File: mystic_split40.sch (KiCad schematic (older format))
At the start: 4 parts

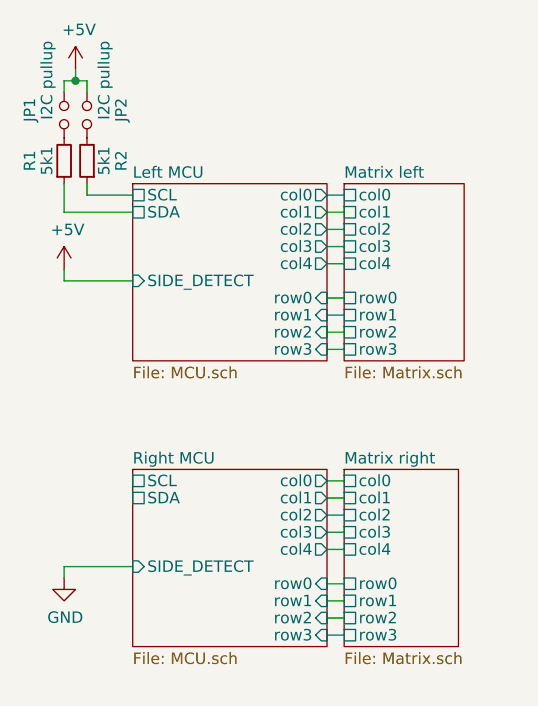
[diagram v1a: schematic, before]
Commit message: Copied left half layout to right components
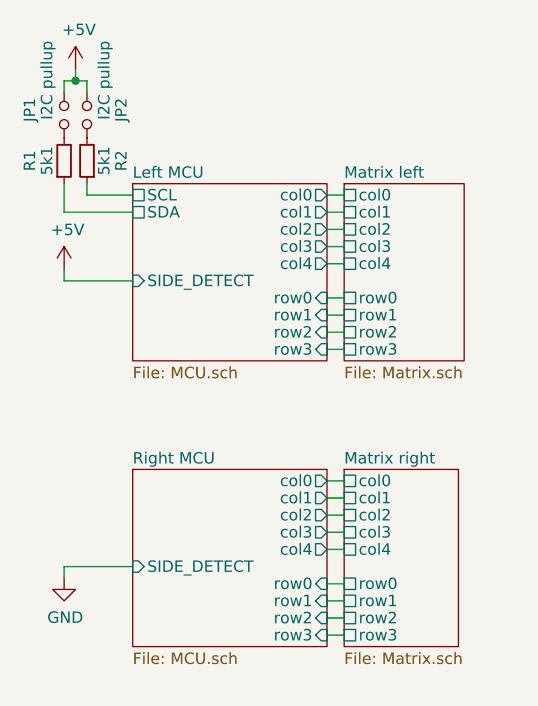
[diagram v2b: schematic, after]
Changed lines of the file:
@@
 F10 "row3" I R 5375 4775 50
 F11 "SIDE_DETECT" I L 4525 4475 50
-F12 "SCL" U L 4525 4100 50
-F13 "SDA" U L 4525 4175 50
 $EndSheet
 $Sheet

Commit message: Started work on adding extra col
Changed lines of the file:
@@
 $EndDescr
-Wire Wire Line
-	5375 3300 5450 3300
 Wire Wire Line
 	5375 3375 5450 3375
@@
 	0    1    1    0
 $EndComp
-$Sheet
-S 4525 2800 850  775
+Wire Wire Line
+	4325 2800 4325 2850
+Wire Wire Line
+	4325 2850 4525 2850
+Wire Wire Line
+	4525 2925 4225 2925
+Wire Wire Line
+	4225 2925 4225 2800
+Wire Wire Line
+	4225 3175 4225 3225
+$Sheet
+S 4525 4050 850  850
+U 5E0F7128
+F0 "Right MCU" 50
+F1 "MCU.sch" 50
+F2 "col0" O R 5375 4100 50
+F3 "col1" O R 5375 4175 50
+F4 "col2" O R 5375 4250 50
+F5 "col3" O R 5375 4325 50
+F6 "col4" O R 5375 4400 50
+F7 "row0" I R 5375 4625 50
+F8 "row1" I R 5375 4700 50
+F9 "row2" I R 5375 4775 50
+F10 "row3" I R 5375 4850 50
+F11 "SIDE_DETECT" I L 4525 4475 50
+F12 "col5" O R 5375 4475 50
+$EndSheet
+$Sheet
+S 5450 2800 525  850
+U 5DBF64D6
+F0 "Matrix left" 50
+F1 "Matrix.sch" 50
+F2 "col0" U L 5450 2850 50
+F3 "col1" U L 5450 2925 50
+F4 "col2" U L 5450 3000 50
+F5 "col3" U L 5450 3075 50
+F6 "col4" U L 5450 3150 50
+F7 "row0" U L 5450 3375 50
+F8 "row1" U L 5450 3450 50
+F9 "row2" U L 5450 3525 50
+F10 "row3" U L 5450 3600 50
+F11 "col5" U L 5450 3225 50
+$EndSheet
+$Sheet
+S 5450 4050 525  850
+U 5E103021
+F0 "Matrix right" 50
+F1 "Matrix.sch" 50
+F2 "col0" U L 5450 4100 50
+F3 "col1" U L 5450 4175 50
+F4 "col2" U L 5450 4250 50
+F5 "col3" U L 5450 4325 50
+F6 "col4" U L 5450 4400 50
+F7 "row0" U L 5450 4625 50
+F8 "row1" U L 5450 4700 50
+F9 "row2" U L 5450 4775 50
+F10 "row3" U L 5450 4850 50
+F11 "col5" U L 5450 4475 50
+$EndSheet
+Wire Wire Line
+	5375 4100 5450 4100
+Wire Wire Line
+	5450 4175 5375 4175
+Wire Wire Line
+	5375 4250 5450 4250
+Wire Wire Line
+	5450 4325 5375 4325
+Wire Wire Line
+	5375 4400 5450 4400
+Wire Wire Line
+	5375 4625 5450 4625
+Wire Wire Line
+	5450 4700 5375 4700
+Wire Wire Line
+	5375 4775 5450 4775
+Wire Wire Line
+	5450 4850 5375 4850
+Wire Wire Line
+	4225 4475 4225 4525
+$Comp
+L power:GND #PWR0103
+U 1 1 5E10A304
+P 4225 4525
+F 0 "#PWR0103" H 4225 4275 50  0001 C CNN
+F 1 "GND" H 4230 4352 50  0000 C CNN
+F 2 "" H 4225 4525 50  0001 C CNN
+F 3 "" H 4225 4525 50  0001 C CNN
+	1    4225 4525
+	1    0    0    -1
+$EndComp
+$Comp
+L power:+5V #PWR0101
+U 1 1 5E29EBF3
+P 4225 3175
+F 0 "#PWR0101" H 4225 3025 50  0001 C CNN
+F 1 "+5V" H 4240 3348 50  0000 C CNN
+F 2 "" H 4225 3175 50  0001 C CNN
+F 3 "" H 4225 3175 50  0001 C CNN
+	1    4225 3175
+	1    0    0    -1
+$EndComp
+$Comp
+L power:+5V #PWR0102
+U 1 1 5E29F27C
+P 4275 2300
+F 0 "#PWR0102" H 4275 2150 50  0001 C CNN
+F 1 "+5V" H 4290 2473 50  0000 C CNN
+F 2 "" H 4275 2300 50  0001 C CNN
+F 3 "" H 4275 2300 50  0001 C CNN
+	1    4275 2300
+	1    0    0    -1
+$EndComp
+Wire Wire Line
+	4225 3225 4525 3225
+Wire Wire Line
+	4225 4475 4525 4475
+$Sheet
+S 4525 2800 850  850
 U 5DCB7F8C
 F0 "Left MCU" 50
@@
 F8 "SCL" U L 4525 2850 50
 F9 "SDA" U L 4525 2925 50
-F10 "row0" I R 5375 3300 50
-F11 "row1" I R 5375 3375 50
-F12 "row2" I R 5375 3450 50
-F13 "row3" I R 5375 3525 50
-$EndSheet
-Wire Wire Line
-	4325 2800 4325 2850
-Wire Wire Line
-	4325 2850 4525 2850
-Wire Wire Line
-	4525 2925 4225 2925
-Wire Wire Line
-	4225 2925 4225 2800
-Wire Wire Line
-	4225 3175 4225 3225
-$Sheet
-S 4525 4050 850  775
-U 5E0F7128
-F0 "Right MCU" 50
-F1 "MCU.sch" 50
-F2 "col0" O R 5375 4100 50
-F3 "col1" O R 5375 4175 50
-F4 "col2" O R 5375 4250 50
-F5 "col3" O R 5375 4325 50
-F6 "col4" O R 5375 4400 50
-F7 "row0" I R 5375 4550 50
-F8 "row1" I R 5375 4625 50
-F9 "row2" I R 5375 4700 50
-F10 "row3" I R 5375 4775 50
-F11 "SIDE_DETECT" I L 4525 4475 50
-$EndSheet
-$Sheet
-S 5450 2800 525  775
-U 5DBF64D6
-F0 "Matrix left" 50
-F1 "Matrix.sch" 50
-F2 "col0" U L 5450 2850 50
-F3 "col1" U L 5450 2925 50
-F4 "col2" U L 5450 3000 50
-F5 "col3" U L 5450 3075 50
-F6 "col4" U L 5450 3150 50
-F7 "row0" U L 5450 3300 50
-F8 "row1" U L 5450 3375 50
-F9 "row2" U L 5450 3450 50
-F10 "row3" U L 5450 3525 50
-$EndSheet
-$Sheet
-S 5450 4050 500  775
-U 5E103021
-F0 "Matrix right" 50
-F1 "Matrix.sch" 50
-F2 "col0" U L 5450 4100 50
-F3 "col1" U L 5450 4175 50
-F4 "col2" U L 5450 4250 50
-F5 "col3" U L 5450 4325 50
-F6 "col4" U L 5450 4400 50
-F7 "row0" U L 5450 4550 50
-F8 "row1" U L 5450 4625 50
-F9 "row2" U L 5450 4700 50
-F10 "row3" U L 5450 4775 50
-$EndSheet
-Wire Wire Line
-	5375 4100 5450 4100
-Wire Wire Line
-	5450 4175 5375 4175
-Wire Wire Line
-	5375 4250 5450 4250
-Wire Wire Line
-	5450 4325 5375 4325
-Wire Wire Line
-	5375 4400 5450 4400
-Wire Wire Line
-	5375 4550 5450 4550
-Wire Wire Line
-	5450 4625 5375 4625
-Wire Wire Line
-	5375 4700 5450 4700
-Wire Wire Line
-	5450 4775 5375 4775
-Wire Wire Line
-	4225 4475 4225 4525
-$Comp
-L power:GND #PWR0103
-U 1 1 5E10A304
-P 4225 4525
-F 0 "#PWR0103" H 4225 4275 50  0001 C CNN
-F 1 "GND" H 4230 4352 50  0000 C CNN
-F 2 "" H 4225 4525 50  0001 C CNN
-F 3 "" H 4225 4525 50  0001 C CNN
-	1    4225 4525
-	1    0    0    -1
-$EndComp
-$Comp
-L power:+5V #PWR0101
-U 1 1 5E29EBF3
-P 4225 3175
-F 0 "#PWR0101" H 4225 3025 50  0001 C CNN
-F 1 "+5V" H 4240 3348 50  0000 C CNN
-F 2 "" H 4225 3175 50  0001 C CNN
-F 3 "" H 4225 3175 50  0001 C CNN
-	1    4225 3175
-	1    0    0    -1
-$EndComp
-$Comp
-L power:+5V #PWR0102
-U 1 1 5E29F27C
-P 4275 2300
-F 0 "#PWR0102" H 4275 2150 50  0001 C CNN
-F 1 "+5V" H 4290 2473 50  0000 C CNN
-F 2 "" H 4275 2300 50  0001 C CNN
-F 3 "" H 4275 2300 50  0001 C CNN
-	1    4275 2300
-	1    0    0    -1
-$EndComp
-Wire Wire Line
-	4225 3225 4525 3225
-Wire Wire Line
-	4225 4475 4525 4475
+F10 "row0" I R 5375 3375 50
+F11 "row1" I R 5375 3450 50
+F12 "row2" I R 5375 3525 50
+F13 "row3" I R 5375 3600 50
+F14 "col5" O R 5375 3225 50
+$EndSheet
+Wire Wire Line
+	5375 3600 5450 3600
+Wire Wire Line
+	5375 4475 5450 4475
+Wire Wire Line
+	5375 3225 5450 3225
 $EndSCHEMATC
